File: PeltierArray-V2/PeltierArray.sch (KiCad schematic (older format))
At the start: 12 parts, among them J1 Barrel_Jack

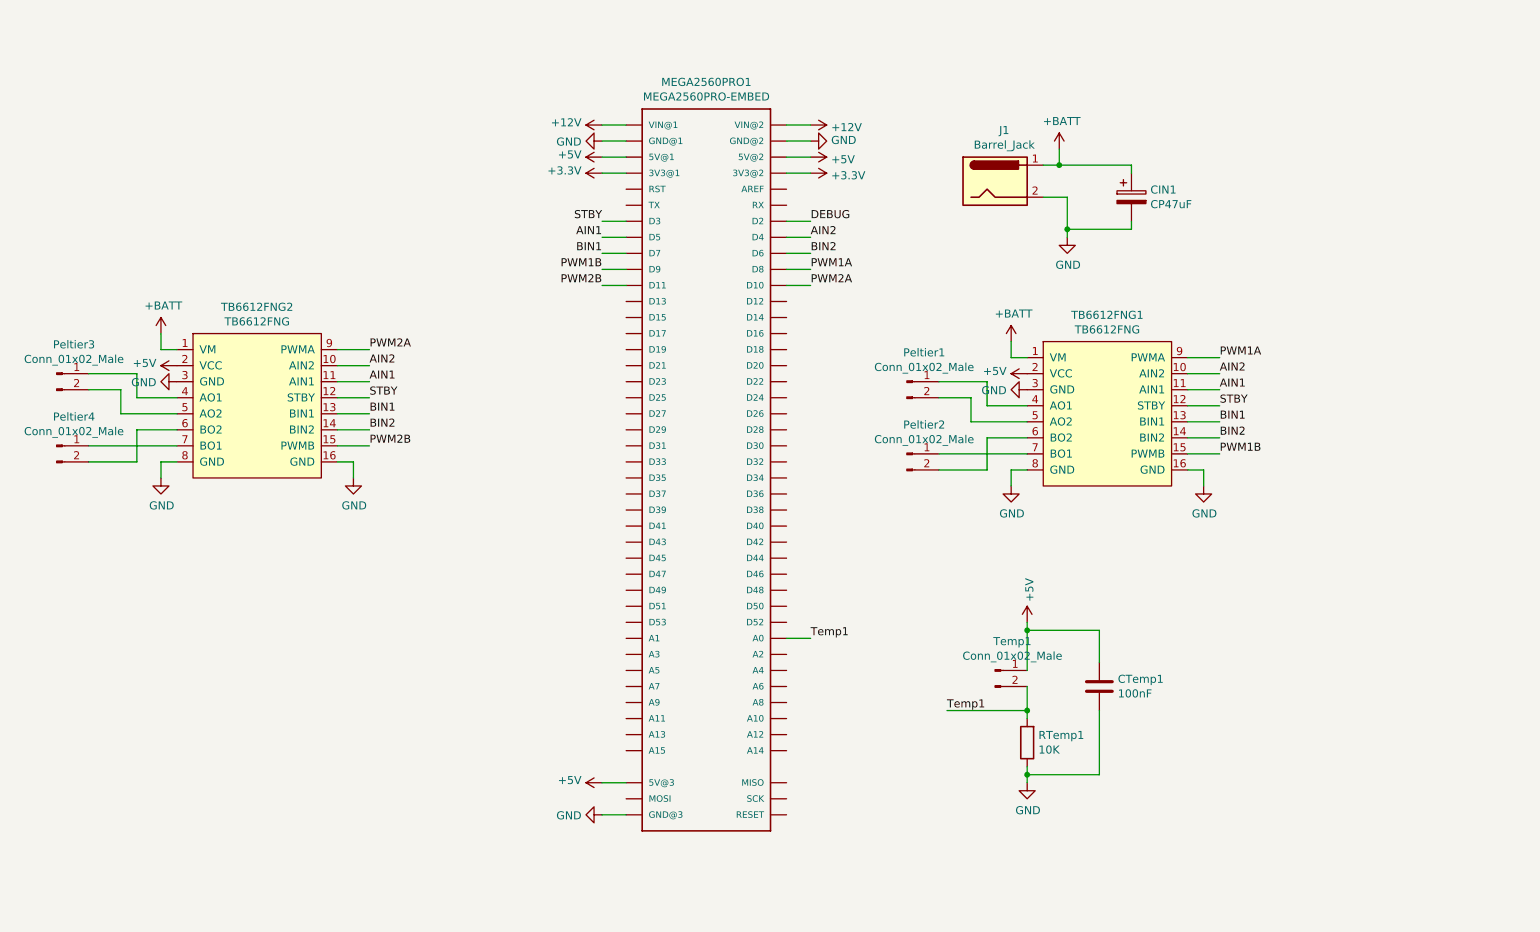
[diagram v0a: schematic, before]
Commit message: Hierarchical schematics
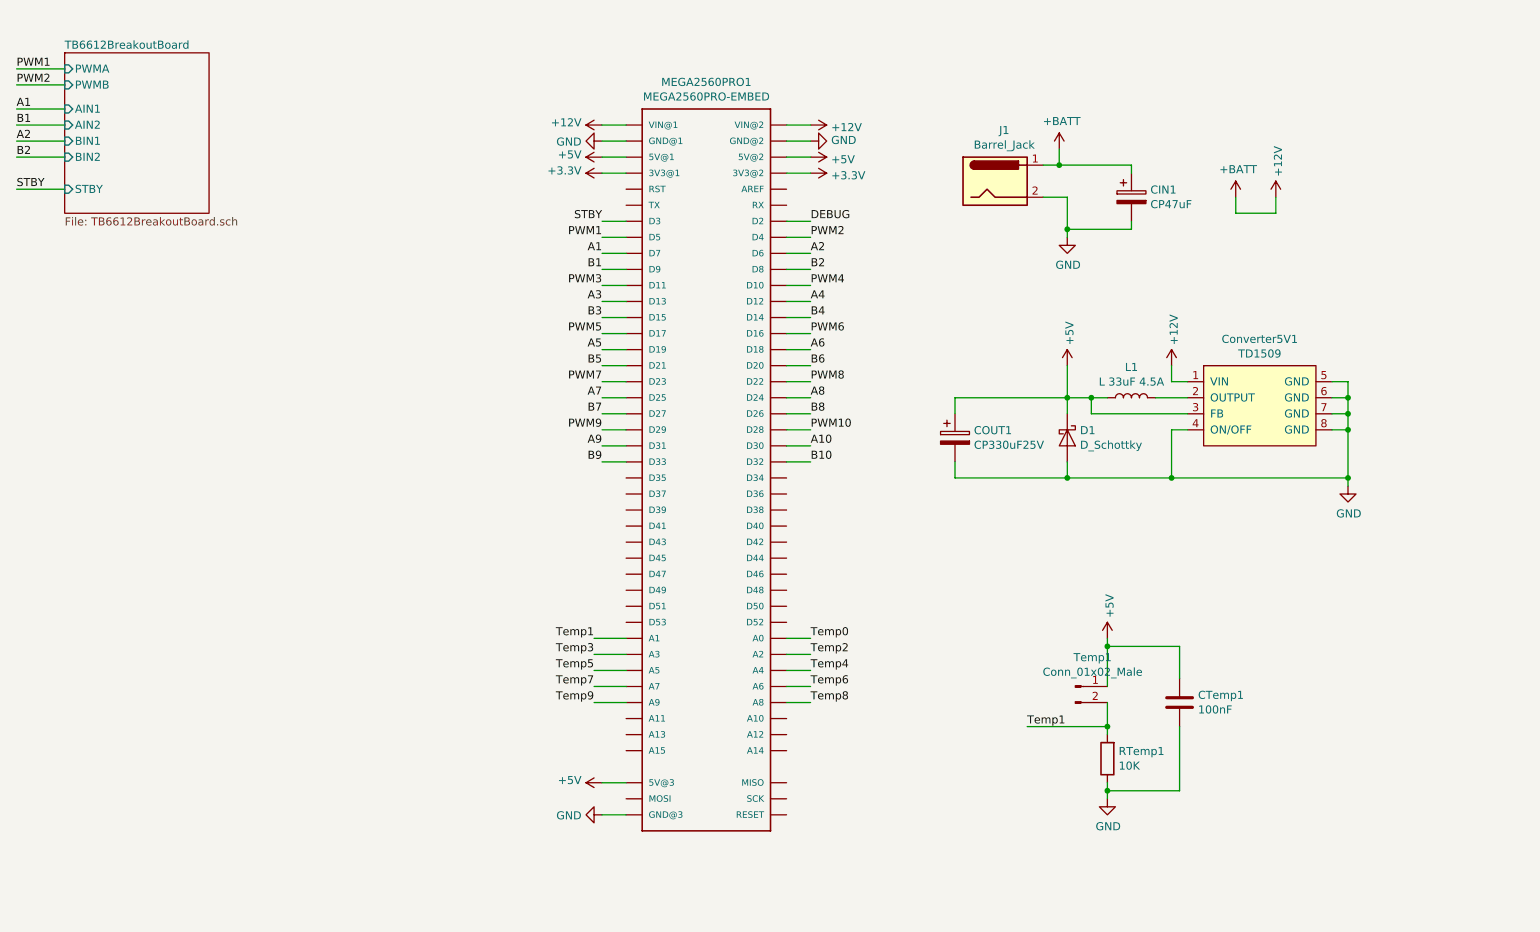
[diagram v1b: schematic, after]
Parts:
- removed Peltier1, Peltier2, Peltier3, Peltier4: Conn_01x02_Male, Connector_JST:JST_PH_B2B-PH-K_1x02_P2.00mm_Vertical, symbol Connector:Conn_01x02_Male
- removed TB6612FNG1, TB6612FNG2: TB6612FNG, PeltierArray:DIP-16_617_ELL, symbol Me-MEGA2560PRO:TB6612FNG
- added COUT1: CP330uF25V, Capacitor_THT:C_Radial_D8.0mm_H11.5mm_P3.50mm, symbol Device:CP
- added Converter5V1: TD1509, Package_SO:SOP-8_3.9x4.9mm_P1.27mm, symbol Me-MEGA2560PRO:TD1509
- added D1: D_Schottky, Diode_SMD:D_SMA, symbol Device:D_Schottky
- added L1: L 33uF 4.5A, Inductor_SMD:L_Taiyo-Yuden_NR-60xx_HandSoldering, symbol Device:L
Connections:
- net +BATT is gone; now on net +12V: CIN1.1, J1.1
- net +12V: now also Converter5V1.1 (VIN)
- net +5V: now also COUT1.1, Converter5V1.3 (FB), D1.1 (K), L1.1
- net GND: now also COUT1.2, Converter5V1.4 (ON/OFF), Converter5V1.5 (GND), Converter5V1.6 (GND), Converter5V1.7 (GND), Converter5V1.8 (GND), D1.2 (A)
- net Temp1: now also MEGA2560PRO1.A1; no longer MEGA2560PRO1.A0
- net Temp2: now reaches MEGA2560PRO1.A2
- net Temp3: now reaches MEGA2560PRO1.A3
- net Temp4: now reaches MEGA2560PRO1.A4
- net Temp5: now reaches MEGA2560PRO1.A5
- net Temp6: now reaches MEGA2560PRO1.A6
- net Temp7: now reaches MEGA2560PRO1.A7
- net Temp8: now reaches MEGA2560PRO1.A8
- net Temp9: now reaches MEGA2560PRO1.A9
- net A4: now reaches MEGA2560PRO1.D12
- net A3: now reaches MEGA2560PRO1.D13
- net B4: now reaches MEGA2560PRO1.D14
- net B3: now reaches MEGA2560PRO1.D15
- net PWM6: now reaches MEGA2560PRO1.D16
- net PWM5: now reaches MEGA2560PRO1.D17
- net A6: now reaches MEGA2560PRO1.D18
- net A5: now reaches MEGA2560PRO1.D19
- net B6: now reaches MEGA2560PRO1.D20
- net B5: now reaches MEGA2560PRO1.D21
- net PWM8: now reaches MEGA2560PRO1.D22
- net PWM7: now reaches MEGA2560PRO1.D23
- net A8: now reaches MEGA2560PRO1.D24
- net A7: now reaches MEGA2560PRO1.D25
- net B8: now reaches MEGA2560PRO1.D26
- net B7: now reaches MEGA2560PRO1.D27
- net PWM10: now reaches MEGA2560PRO1.D28
- net PWM9: now reaches MEGA2560PRO1.D29
- net A10: now reaches MEGA2560PRO1.D30
- net A9: now reaches MEGA2560PRO1.D31
- net B10: now reaches MEGA2560PRO1.D32
- net B9: now reaches MEGA2560PRO1.D33
- net AIN1 renamed PWM1
- net AIN2 renamed PWM2
- net BIN1 renamed A1
- net BIN2 renamed A2
- net PWM1A renamed B2
- net PWM1B renamed B1
- net PWM2A renamed PWM4
- net PWM2B renamed PWM3
- new net: Converter5V1.2 (OUTPUT), L1.2
- new net Temp0: MEGA2560PRO1.A0
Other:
- moved on the sheet: CTemp1, RTemp1, Temp1

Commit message: TB6612
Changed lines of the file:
@@
 Wire Wire Line
 	5000 2150 4850 2150
-Wire Wire Line
-	5000 2050 4850 2050
-Text Label 4850 2050 2    50   ~ 0
-STBY
 Text Label 6150 2050 0    50   ~ 0
 DEBUG
@@
 	7050 3650 7750 3650
 Connection ~ 7750 3650
-$Sheet
-S 1500 1000 900  1000
-U 5F888F89
-F0 "TB6612BreakoutBoard" 50
-F1 "TB6612BreakoutBoard.sch" 50
-F2 "PWMA" I L 1500 1100 50
-F3 "AIN2" I L 1500 1450 50
-F4 "AIN1" I L 1500 1350 50
-F5 "STBY" I L 1500 1850 50
-F6 "BIN1" I L 1500 1550 50
-F7 "BIN2" I L 1500 1650 50
-F8 "PWMB" I L 1500 1200 50
-$EndSheet
 Wire Wire Line
 	1500 1100 1200 1100
@@
 Wire Wire Line
 	1500 1650 1200 1650
-Wire Wire Line
-	1500 1850 1200 1850
 Text Label 1200 1100 0    50   ~ 0
 PWM1
@@
 Text Label 1200 1450 0    50   ~ 0
 B1
-Text Label 1200 1850 0    50   ~ 0
-STBY
 Wire Wire Line
 	6000 2550 6150 2550
@@
 Wire Wire Line
 	6000 4650 6150 4650
+Text GLabel 4600 2050 0    50   Input ~ 0
+STBY
+Wire Wire Line
+	4600 2050 5000 2050
+$Sheet
+S 1500 1000 550  750
+U 5F888F89
+F0 "TB6612" 50
+F1 "TB6612.sch" 50
+F2 "PWMA" I L 1500 1100 50
+F3 "AIN2" I L 1500 1450 50
+F4 "AIN1" I L 1500 1350 50
+F5 "BIN1" I L 1500 1550 50
+F6 "BIN2" I L 1500 1650 50
+F7 "PWMB" I L 1500 1200 50
+$EndSheet
 $EndSCHEMATC

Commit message: UART I2C
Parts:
- removed CTemp1: 100nF, Capacitor_SMD:C_0603_1608Metric, symbol Device:C
- removed RTemp1: 10K, Resistors:0603, symbol Device:R
- removed Temp1: Conn_01x02_Male, Connector_JST:JST_XH_B2B-XH-A_1x02_P2.50mm_Vertical, symbol Connector:Conn_01x02_Male
- added COUT2: CP330uF25V, Capacitor_THT:C_Radial_D8.0mm_H11.5mm_P3.50mm, symbol Device:CP
- added Converter5V2: TD1509, Package_SO:SOP-8_3.9x4.9mm_P1.27mm, symbol Me-MEGA2560PRO:TD1509
- added D2: D_Schottky, Diode_SMD:D_SMA, symbol Device:D_Schottky
- added I2C1, UART1: Conn_01x04_Male, Connector_JST:JST_PH_B4B-PH-K_1x04_P2.00mm_Vertical, symbol Connector:Conn_01x04_Male
- added L2: L 33uF 4.5A, Inductor_SMD:L_Taiyo-Yuden_NR-60xx_HandSoldering, symbol Device:L
- added SYNC1: Conn_01x02_Male, Connector_JST:JST_PH_B2B-PH-K_1x02_P2.00mm_Vertical, symbol Connector:Conn_01x02_Male
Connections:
- net +12V: now also Converter5V2.1 (VIN)
- net +5V: now also COUT2.1, Converter5V2.3 (FB), D2.1 (K), L2.1
- net A1: now also MEGA2560PRO1.D25; no longer MEGA2560PRO1.D7
- net A10: now also MEGA2560PRO1.D48; no longer MEGA2560PRO1.D30
- net A2: now also MEGA2560PRO1.D24; no longer MEGA2560PRO1.D6
- net A3: now also MEGA2560PRO1.D31; no longer MEGA2560PRO1.D13
- net A4: now also MEGA2560PRO1.D30; no longer MEGA2560PRO1.D12
- net A5: now also MEGA2560PRO1.D37; no longer MEGA2560PRO1.D19
- net A6: now also MEGA2560PRO1.D36; no longer MEGA2560PRO1.D18
- net A7: now also MEGA2560PRO1.D43; no longer MEGA2560PRO1.D25
- net A8: now also MEGA2560PRO1.D42; no longer MEGA2560PRO1.D24
- net A9: now also MEGA2560PRO1.D49; no longer MEGA2560PRO1.D31
- net B1: now also MEGA2560PRO1.D27; no longer MEGA2560PRO1.D9
- net B10: now also MEGA2560PRO1.D50; no longer MEGA2560PRO1.D32
- net B2: now also MEGA2560PRO1.D26; no longer MEGA2560PRO1.D8
- net B3: now also MEGA2560PRO1.D33; no longer MEGA2560PRO1.D15
- net B4: now also MEGA2560PRO1.D32; no longer MEGA2560PRO1.D14
- net B5: now also MEGA2560PRO1.D39; no longer MEGA2560PRO1.D21
- net B6: now also MEGA2560PRO1.D38; no longer MEGA2560PRO1.D20
- net B7: now also MEGA2560PRO1.D45; no longer MEGA2560PRO1.D27
- net B8: now also MEGA2560PRO1.D44; no longer MEGA2560PRO1.D26
- net B9: now also MEGA2560PRO1.D51; no longer MEGA2560PRO1.D33
- net GND: now also COUT2.2, Converter5V2.4 (ON/OFF), Converter5V2.5 (GND), Converter5V2.6 (GND), Converter5V2.7 (GND), Converter5V2.8 (GND), D2.2 (A), I2C1.2 (Pin_2), SYNC1.2 (Pin_2), UART1.2 (Pin_2)
- net PWM1: now also MEGA2560PRO1.D23; no longer MEGA2560PRO1.D5
- net PWM10: now also MEGA2560PRO1.D46; no longer MEGA2560PRO1.D28
- net PWM2: now also MEGA2560PRO1.D22; no longer MEGA2560PRO1.D4
- net PWM3: now also MEGA2560PRO1.D29; no longer MEGA2560PRO1.D11
- net PWM4: now also MEGA2560PRO1.D28; no longer MEGA2560PRO1.D10
- net PWM5: now also MEGA2560PRO1.D35; no longer MEGA2560PRO1.D17
- net PWM6: now also MEGA2560PRO1.D34; no longer MEGA2560PRO1.D16
- net PWM7: now also MEGA2560PRO1.D41; no longer MEGA2560PRO1.D23
- net PWM8: now also MEGA2560PRO1.D40; no longer MEGA2560PRO1.D22
- net PWM9: now also MEGA2560PRO1.D47; no longer MEGA2560PRO1.D29
- new net: Converter5V2.2 (OUTPUT), L2.2
- new net RX1: MEGA2560PRO1.D19, UART1.4 (Pin_4)
- new net RX2: MEGA2560PRO1.D17
- new net RX3: MEGA2560PRO1.D15
- new net SCL: I2C1.3 (Pin_3), MEGA2560PRO1.D21
- new net SDA: I2C1.4 (Pin_4), MEGA2560PRO1.D20
- new net SYNC: MEGA2560PRO1.D4, SYNC1.1 (Pin_1)
- new net TX1: MEGA2560PRO1.D18, UART1.3 (Pin_3)
- new net TX2: MEGA2560PRO1.D16
- new net TX3: MEGA2560PRO1.D14
- new net VDD: I2C1.1 (Pin_1), UART1.1 (Pin_1)

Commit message: BeginRoute
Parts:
- removed I2C1, UART1: Conn_01x04_Male, Connector_JST:JST_PH_B4B-PH-K_1x04_P2.00mm_Vertical, symbol Connector:Conn_01x04_Male
- added D6, D7, I2C1, SYNC2, UART1: Conn_01x02_Male, Connector_JST:JST_XH_B2B-XH-A_1x02_P2.50mm_Vertical, symbol Connector:Conn_01x02_Male
- SYNC1: footprint Connector_JST:JST_PH_B2B-PH-K_1x02_P2.00mm_Vertical -> Connector_JST:JST_XH_B2B-XH-A_1x02_P2.50mm_Vertical
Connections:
- net GND: now also D6.2 (Pin_2), D7.2 (Pin_2), SYNC2.2 (Pin_2)
- net RX1: now also UART1.2 (Pin_2)
- net SCL: now also I2C1.1 (Pin_1)
- net SDA: now also I2C1.2 (Pin_2)
- net TX1: now also UART1.1 (Pin_1)
- net SYNC2: now reaches MEGA2560PRO1.D5
- net SYNC2: now also SYNC2.1 (Pin_1)
- net D6: now reaches MEGA2560PRO1.D6
- net D6: now also D6.1 (Pin_1)
- net D7: now reaches MEGA2560PRO1.D7
- net D7: now also D7.1 (Pin_1)
- net SYNC renamed SYNC1
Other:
- moved on the sheet: SYNC1

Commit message: FUUUUUUCK
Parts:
- renumbered D6 to D3, D7 to D4

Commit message: FinishRoute
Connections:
- net +12V: no longer MEGA2560PRO1.VIN@1, MEGA2560PRO1.VIN@2
- no-connect marks 0 -> 2
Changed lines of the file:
@@
 Wire Wire Line
 	6000 1650 6150 1650
-$Comp
-L power:+12V #PWR02
-U 1 1 5F88167A
-P 6150 1450
-F 0 "#PWR02" H 6150 1300 50  0001 C CNN
-F 1 "+12V" V 6165 1578 50  0000 L CNN
-F 2 "" H 6150 1450 50  0001 C CNN
-F 3 "" H 6150 1450 50  0001 C CNN
-	1    6150 1450
-	0    1    1    0
-$EndComp
-$Comp
-L power:+12V #PWR01
-U 1 1 5F882BE5
-P 4850 1450
-F 0 "#PWR01" H 4850 1300 50  0001 C CNN
-F 1 "+12V" V 4865 1578 50  0000 L CNN
-F 2 "" H 4850 1450 50  0001 C CNN
-F 3 "" H 4850 1450 50  0001 C CNN
-	1    4850 1450
-	0    -1   -1   0
-$EndComp
 Wire Wire Line
 	4850 1450 5000 1450
@@
 Text Label 9600 6250 0    50   ~ 0
 D7
+NoConn ~ 6150 1450
+NoConn ~ 4850 1450
 $EndSCHEMATC
